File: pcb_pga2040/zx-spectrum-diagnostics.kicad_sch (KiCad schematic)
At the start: 20 parts, among them J101 Conn_01x04, J102 Conn_01x03_Male, J103 Conn_01x03_Male, Q101 PMBT2222A, SW101 SW_SPST, SW102 SW_SPST, U101 Pico, U102 Pico, U103 PGA2040

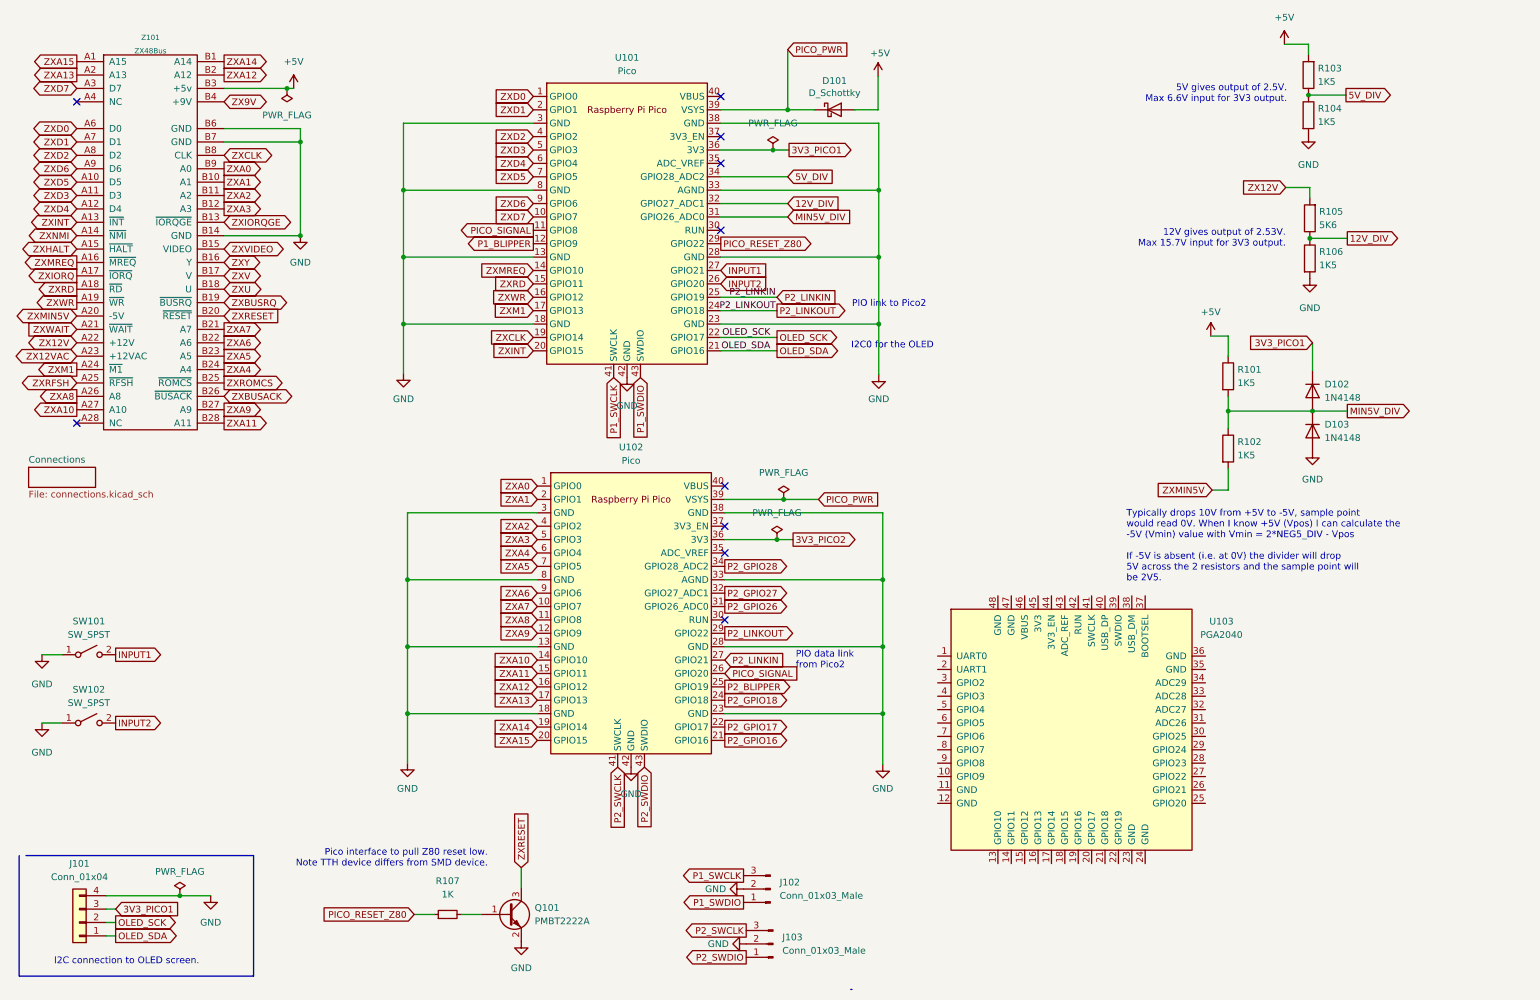
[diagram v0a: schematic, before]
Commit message: update v1.2 pcb, add comments to PGS version, create v1.2 gerbers
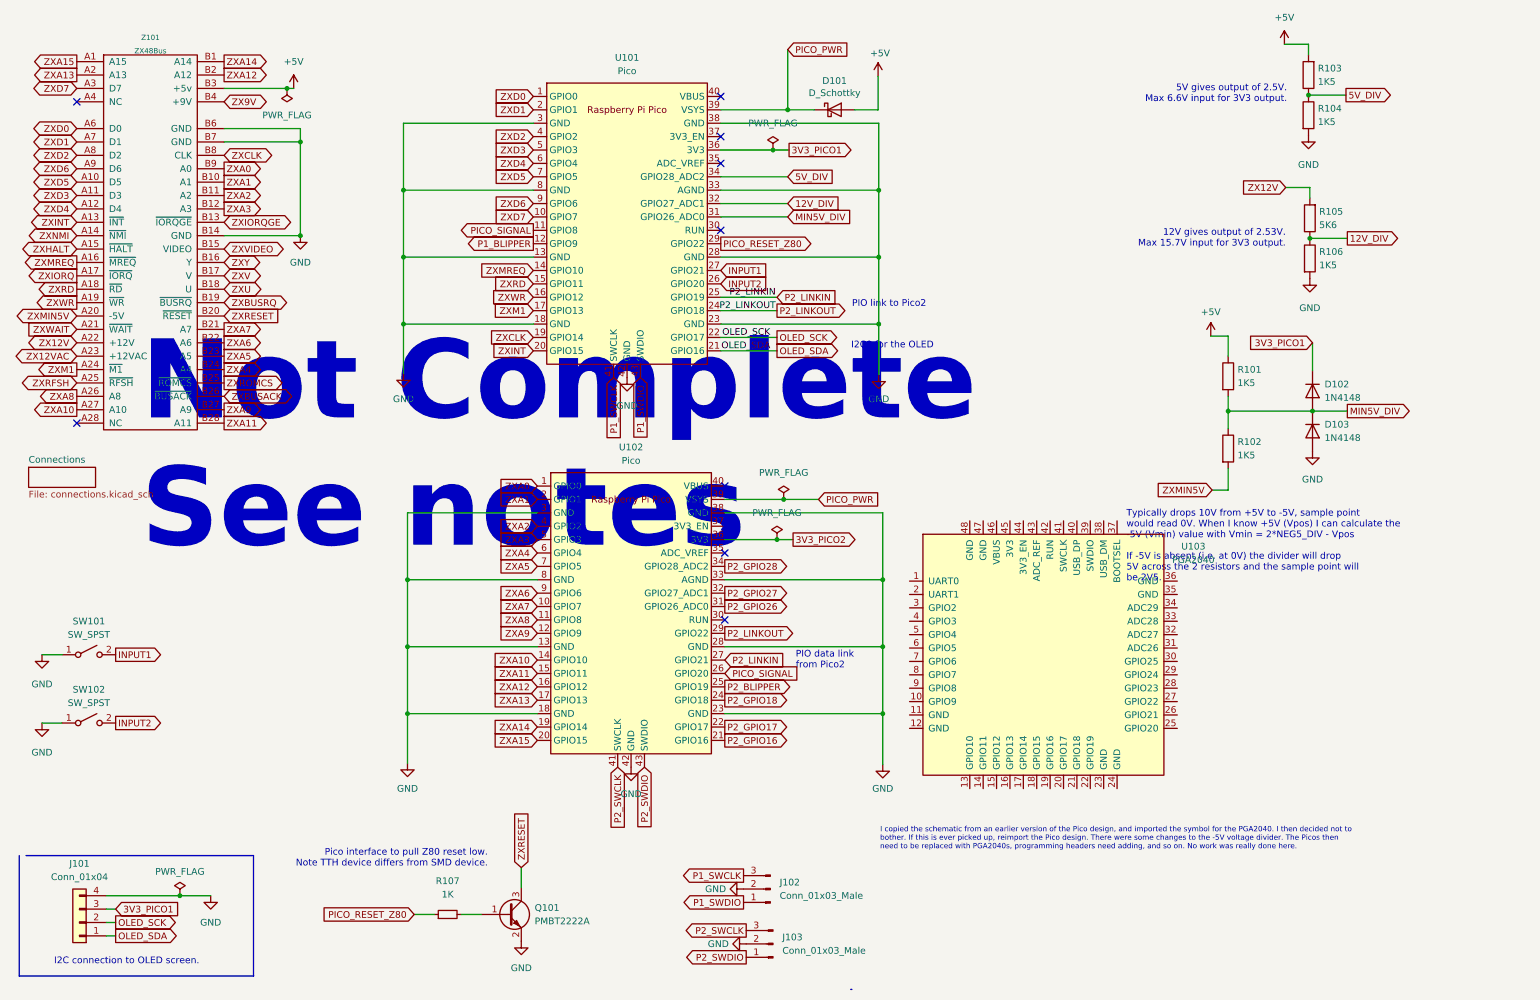
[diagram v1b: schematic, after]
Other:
- note added: "I copied the schematic from an earlier version of the Pico design, and imported the symbol for the PGA2040. I then decided not to bother. If this is ever picked up, reimport the Pico design. There were some changes to the -5V voltage divider. The Picos then need to be replaced with PGA2040s, programming headers need adding, and so on. No work was really done here."
- note added: "Not Complete See notes"
- moved on the sheet: U103
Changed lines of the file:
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@@
   (title_block
     (title "ZX Spectrum Diagnostics Board PGA2040")
-    (date "2024-02-19")
+    (date "2024-03-12")
   )
   (junction (at 67.818 37.592) (diameter 0) (color 0 0 0 0)
@@
     (at 103.378 175.26 180)
     (effects (font (size 1.27 1.27)) (justify right bottom))
+  )
+  (text "Not Complete\nSee notes" (at 37.592 116.078 0)
+    (effects (font (size 15 15) (thickness 3) bold) (justify left bottom))
+  )
+  (text "I copied the schematic from an earlier version of the Pico design, and imported the symbol for the PGA2040. I then decided not to\nbother. If this is ever picked up, reimport the Pico design. There were some changes to the -5V voltage divider. The Picos then\nneed to be replaced with PGA2040s, programming headers need adding, and so on. No work was really done here."
+    (at 177.8 171.958 0)
+    (effects (font (size 1 1)) (justify left bottom))
   )
   (text "Typically drops 10V from +5V to -5V, sample point\nwould read 0V. When I know +5V (Vpos) I can calculate the\n-5V (Vmin) value with Vmin = 2*NEG5_DIV - Vpos\n\nIf -5V is absent (i.e. at 0V) the divider will drop\n5V across the 2 resistors and the sample point will\nbe 2V5."
@@
     (pin "1")
   )
-  (symbol (lib_id "PGA2404:PGA2040") (at 214.122 149.098 0) (unit 1)
+  (symbol (lib_id "PGA2404:PGA2040") (at 208.788 134.874 0) (unit 1)
     (in_bom yes) (on_board yes) (fields_autoplaced)
-    (property "Reference" "U103" (id 0) (at 242.57 128.5492 0))
-    (property "Value" "PGA2040" (id 1) (at 242.57 131.0892 0))
-    (property "Footprint" "PGA2040:PGA2040" (id 2) (at 214.122 149.098 0)
-      (effects (font (size 1.27 1.27)) hide)
-    )
-    (property "Datasheet" "" (id 3) (at 197.612 142.748 0)
-      (effects (font (size 1.27 1.27)) hide)
-    )
+    (property "Reference" "U103" (id 0) (at 237.236 114.3252 0))
+    (property "Value" "PGA2040" (id 1) (at 237.236 116.8652 0))
+    (property "Footprint" "PGA2040:PGA2040" (id 2) (at 208.788 134.874 0)
+      (effects (font (size 1.27 1.27)) hide)
+    )
+    (property "Datasheet" "" (id 3) (at 192.278 128.524 0)
+      (effects (font (size 1.27 1.27)) hide)
+    )
